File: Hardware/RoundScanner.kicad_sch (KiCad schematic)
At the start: 0 parts

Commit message: Version 0.1
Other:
- sheet Sensor renamed InGaS Sensor

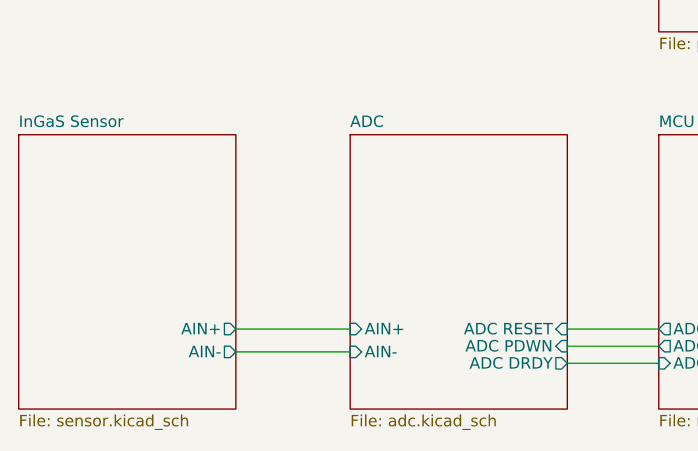
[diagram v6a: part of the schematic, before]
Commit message: initial branch commit with rought layout changes
Signed-off-by: Lawrence Kincheloe <lawrence.kincheloe@mavericktechok.com>
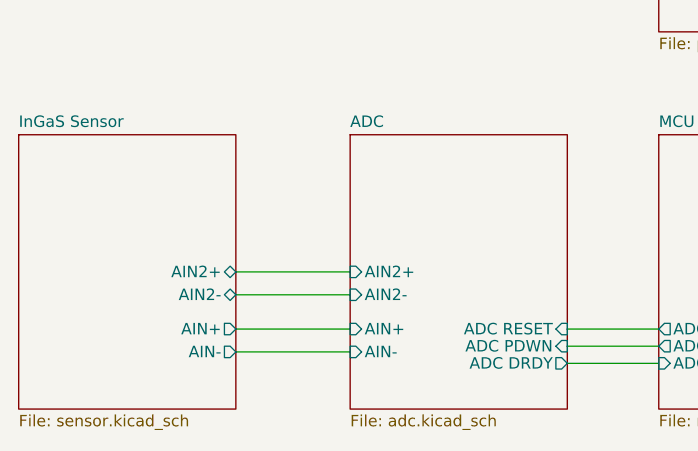
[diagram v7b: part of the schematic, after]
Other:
- sheet ADC ports: added AIN2+, AIN2-; removed none
- sheet InGaS Sensor ports: added AIN2+, AIN2-; removed none
